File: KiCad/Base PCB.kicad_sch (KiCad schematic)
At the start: 8 parts, among them J201 Conn_02x32_Odd_Even, J202 Conn_02x20_Odd_Even

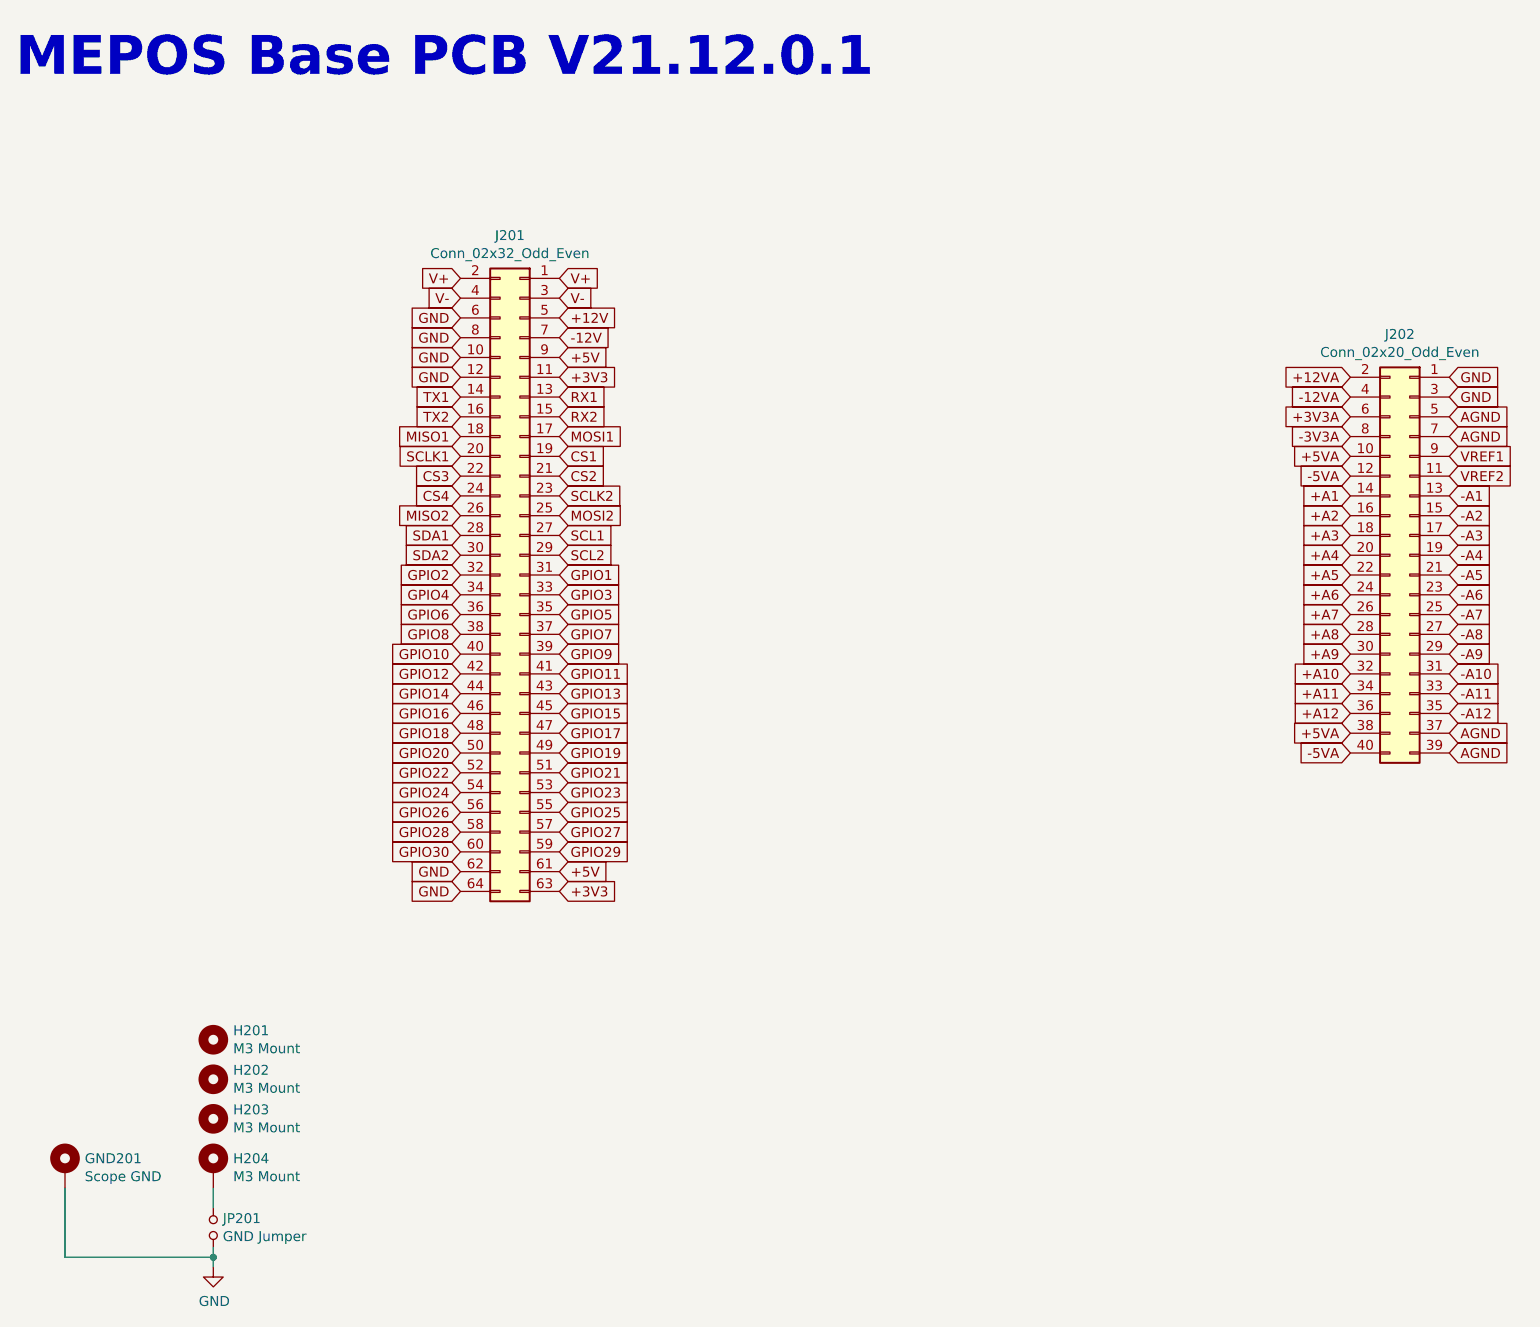
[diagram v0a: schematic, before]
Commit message: Updated to MEPOS V0.2
updated pcb
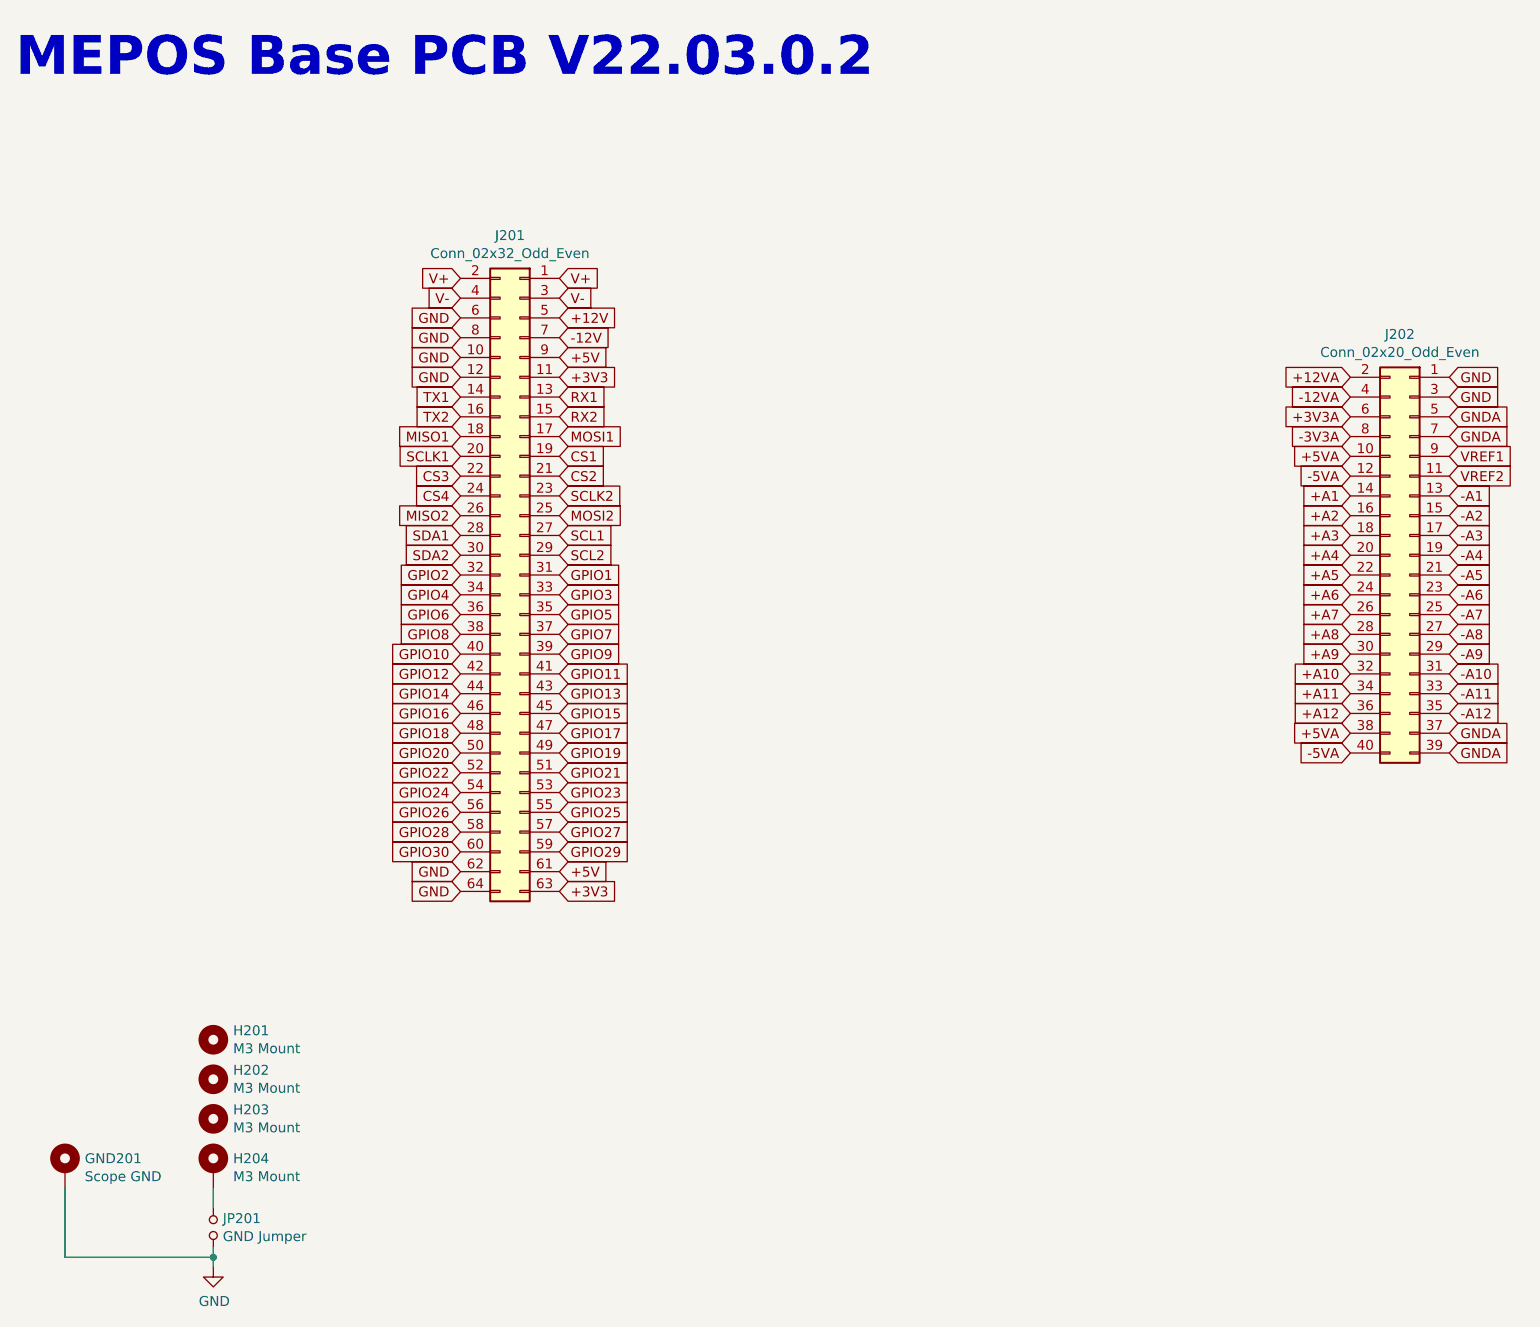
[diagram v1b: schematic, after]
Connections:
- net AGND renamed GNDA
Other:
- note added: "MEPOS Base PCB V22.03.0.2"
- note removed: "MEPOS Base PCB V21.12.0.1"
- title: MEPOS Base PCB V21.12.0.1 -> MEPOS Base PCB
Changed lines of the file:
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@@
   (paper "A4")
   (title_block
-    (title "MEPOS Base PCB V21.12.0.1")
-    (date "2021-12-17")
-    (rev "V21.12.0.1")
+    (title "MEPOS Base PCB")
+    (date "2022-03-21")
+    (rev "V22.03.0.2")
   )
   (junction (at 50.8 176.53) (diameter 0) (color 0 0 0 0)
@@
     (stroke (width 0) (type default) (color 0 0 0 0))
   )
-  (text "MEPOS Base PCB V21.12.0.1" (at 25.4 25.4 0)
+  (text "MEPOS Base PCB V22.03.0.2" (at 25.4 25.4 0)
     (effects (font (size 5.0038 5.0038) (thickness 1.0008) bold) (justify left bottom))
   )
@@
     )
   )
-  (global_label "AGND" (shape input) (at 209.55 71.12 0) (fields_autoplaced)
-    (effects (font (size 1.27 1.27)) (justify left))
-    (property "Intersheet References" "${INTERSHEET_REFS}" (id 0) (at 0 0 0)
-      (effects (font (size 1.27 1.27)) hide)
+  (global_label "GNDA" (shape input) (at 209.55 71.12 0) (fields_autoplaced)
+    (effects (font (size 1.27 1.27)) (justify left))
+    (property "Intersheet References" "${INTERSHEET_REFS}" (id 0) (at 216.8332 71.0406 0)
+      (effects (font (size 1.27 1.27)) (justify left) hide)
     )
   )
@@
     )
   )
-  (global_label "AGND" (shape input) (at 209.55 111.76 0) (fields_autoplaced)
-    (effects (font (size 1.27 1.27)) (justify left))
-    (property "Intersheet References" "${INTERSHEET_REFS}" (id 0) (at 0 0 0)
-      (effects (font (size 1.27 1.27)) hide)
+  (global_label "GNDA" (shape input) (at 209.55 111.76 0) (fields_autoplaced)
+    (effects (font (size 1.27 1.27)) (justify left))
+    (property "Intersheet References" "${INTERSHEET_REFS}" (id 0) (at 216.8332 111.6806 0)
+      (effects (font (size 1.27 1.27)) (justify left) hide)
     )
   )
@@
     )
   )
-  (global_label "AGND" (shape input) (at 209.55 68.58 0) (fields_autoplaced)
-    (effects (font (size 1.27 1.27)) (justify left))
-    (property "Intersheet References" "${INTERSHEET_REFS}" (id 0) (at 0 0 0)
-      (effects (font (size 1.27 1.27)) hide)
+  (global_label "GNDA" (shape input) (at 209.55 68.58 0) (fields_autoplaced)
+    (effects (font (size 1.27 1.27)) (justify left))
+    (property "Intersheet References" "${INTERSHEET_REFS}" (id 0) (at 216.8332 68.5006 0)
+      (effects (font (size 1.27 1.27)) (justify left) hide)
     )
   )
@@
     )
   )
-  (global_label "AGND" (shape input) (at 209.55 109.22 0) (fields_autoplaced)
-    (effects (font (size 1.27 1.27)) (justify left))
-    (property "Intersheet References" "${INTERSHEET_REFS}" (id 0) (at 0 0 0)
-      (effects (font (size 1.27 1.27)) hide)
-    )
-  )
+  (global_label "GNDA" (shape input) (at 209.55 109.22 0) (fields_autoplaced)
+    (effects (font (size 1.27 1.27)) (justify left))
+    (property "Intersheet References" "${INTERSHEET_REFS}" (id 0) (at 216.8332 109.1406 0)
+      (effects (font (size 1.27 1.27)) (justify left) hide)
+    )
+  )

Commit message: Updated to MEPOS V0.3
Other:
- note added: "MEPOS Base PCB V22.04.0.3"
- note removed: "MEPOS Base PCB V22.03.0.2"
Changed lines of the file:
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@@
   (title_block
     (title "MEPOS Base PCB")
-    (date "2022-03-21")
-    (rev "V22.03.0.2")
+    (date "2022-04-13")
+    (rev "V22.04.0.3")
   )
   (junction (at 50.8 176.53) (diameter 0) (color 0 0 0 0)
@@
     (stroke (width 0) (type default) (color 0 0 0 0))
   )
-  (text "MEPOS Base PCB V22.03.0.2" (at 25.4 25.4 0)
+  (text "MEPOS Base PCB V22.04.0.3" (at 25.4 25.4 0)
     (effects (font (size 5.0038 5.0038) (thickness 1.0008) bold) (justify left bottom))
   )
